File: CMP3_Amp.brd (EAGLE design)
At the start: 100 x 80 mm, 22 parts, among them J1 CONN_42.54_SCREW, J2 CONN_33.5_SCREW, Q2 DMG3404, U1 LTC2054, U2 LTC2054

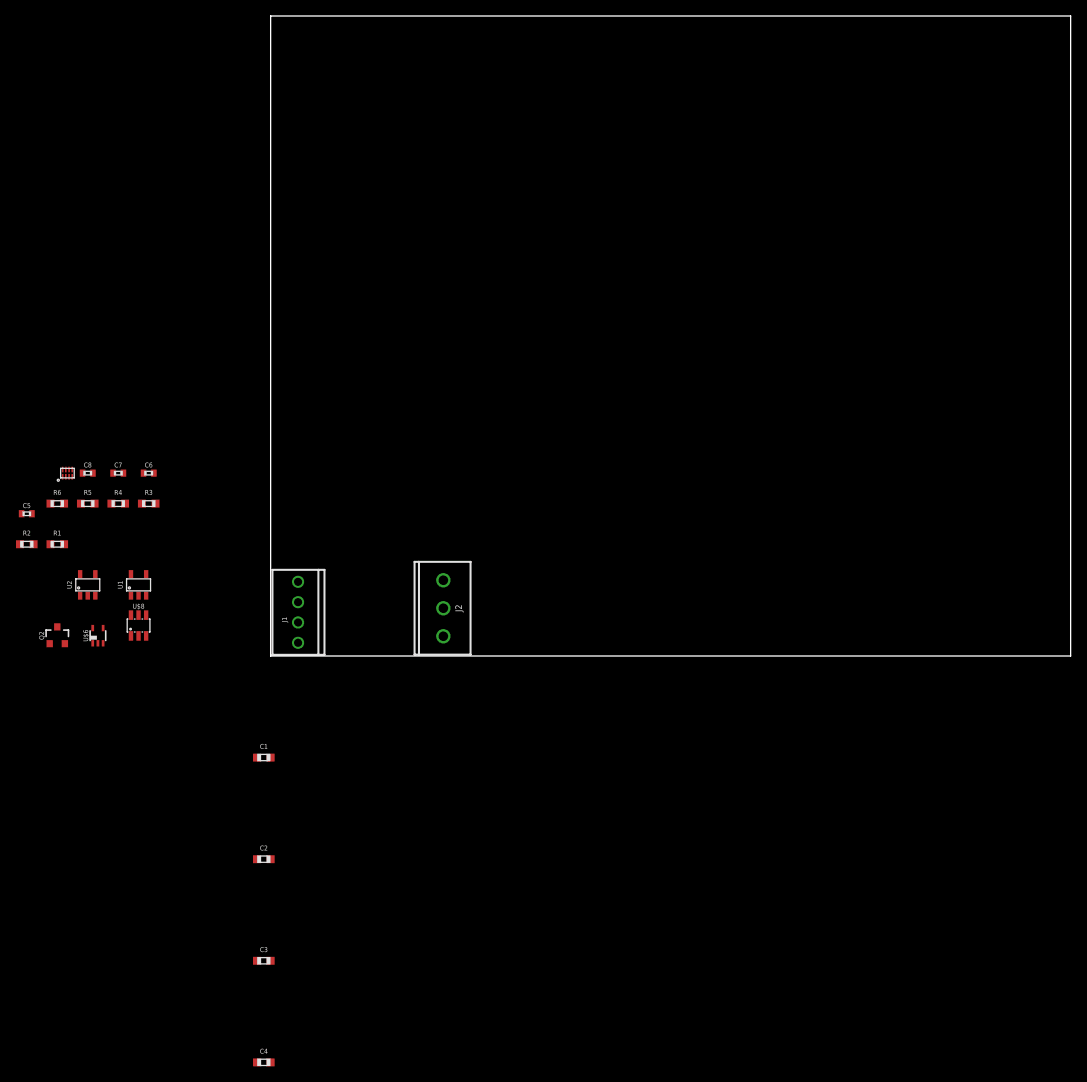
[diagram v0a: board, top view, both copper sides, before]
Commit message: Initial layout of CMP3 Amp
Layout of CMP3 amp complete, requires review and gerber generation before being sent to fab
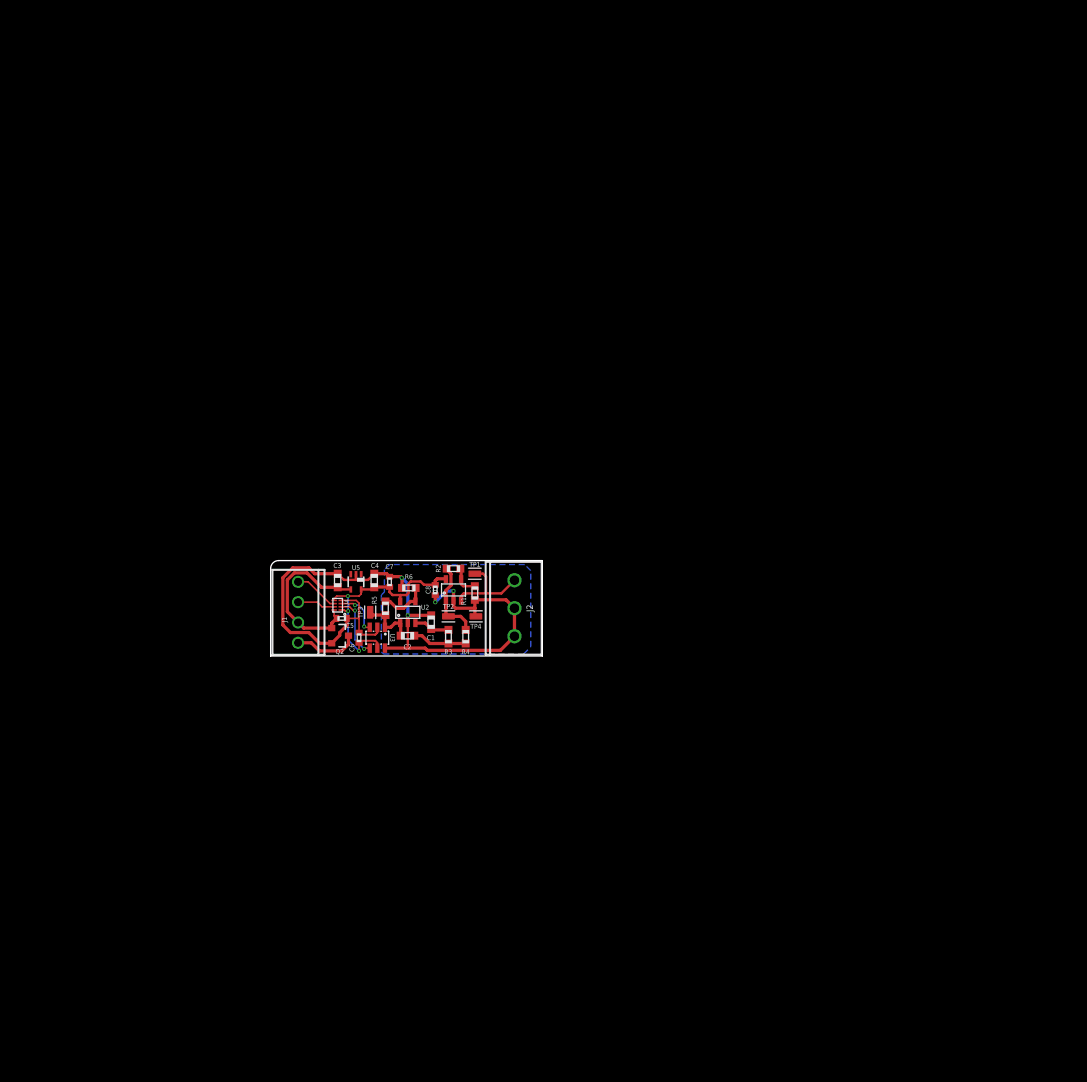
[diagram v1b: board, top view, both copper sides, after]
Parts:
- removed U$3: TXS0102DQM, bschulz:DQM_R-PX2SON-N8
- removed U$6: TPS79733, bschulz:DCK_R-PDSO-G5
- removed U$8: MCP3421A1, bschulz:SOT23-6L
- added TP1, TP2, TP3, TP4: TESTPOINTRCU, bschulz:TESTPOINT_0603
- added U3: MCP3421A1, bschulz:SOT23-6L
- added U4: TXS0102DQM, bschulz:DQM_R-PX2SON-N8
- added U5: TPS79733, bschulz:DCK_R-PDSO-G5
- moved C4 61.8 mm to (13.0, 9.44), turned to 90 degrees
- moved R2 53.4 mm to (22.9, 10.9)
- moved R1 52.6 mm to (25.5, 7.87), turned to 90 degrees
- moved C3 48.4 mm to (8.38, 9.44), turned to 90 degrees
- moved C8 45.8 mm to (20.6, 8.26), turned to 270 degrees
- moved R6 45.2 mm to (17.3, 8.51)
- moved R4 44.5 mm to (22.2, 2.41), turned to 270 degrees
- moved R3 43.0 mm to (24.4, 2.41), turned to 90 degrees
- moved C5 41.5 mm to (8.89, 4.70)
- moved U2 40.2 mm to (17.1, 5.46)
- moved R5 39.4 mm to (14.4, 5.97), turned to 270 degrees
- moved U1 39.4 mm to (22.9, 8.26)
- moved C7 36.5 mm to (14.9, 9.27), turned to 90 degrees
- moved Q2 35.3 mm to (8.64, 2.54), turned to 270 degrees
- moved C6 33.4 mm to (11.0, 2.29), turned to 90 degrees
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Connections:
- net 3V3: now also U3.5, U4.1, U4.5, U5.5; no longer U$3.1, U$3.5, U$6.5, U$8.5
- net GND: now also TP4.1, U3.2, U3.6, U4.4, U5.2; no longer U$3.4, U$6.2, U$8.2, U$8.6
- net SCL: now also U3.3, U4.3; no longer U$3.2, U$8.3
- net SCL_HV: now also U4.6; no longer U$3.7
- net SDA: now also U3.4, U4.2; no longer U$3.3, U$8.4
- net SDA_HV: now also U4.7; no longer U$3.6
- net VIN+: now also U4.8, U5.4; no longer U$3.8, U$6.4
- net VOUT_FILT: now also TP3.1, U3.1; no longer U$8.1
- net VOUT_GAIN: now also TP2.1
- net V_PYRO: now also TP1.1
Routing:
- net GND: track 0.00 -> 94.7 mm, vias 0 -> 4
- net 3V3: track 0.00 -> 31.4 mm, vias 0 -> 3
- net VIN+: track 0.00 -> 22.2 mm
- net V_PYRO: track 0.00 -> 11.7 mm
- net VOUT_GAIN: track 0.00 -> 10.1 mm
- net VIN-: track 0.00 -> 8.14 mm
- net SDA: track 0.00 -> 7.91 mm, vias 0 -> 2
- net VOUT_FILT: track 0.00 -> 7.33 mm
- net N$5: track 0.00 -> 6.83 mm
- net V_FB: track 0.00 -> 6.17 mm
- net SCL: track 0.00 -> 5.93 mm, vias 0 -> 2
- net SCL_HV: track 0.00 -> 5.63 mm
- net SDA_HV: track 0.00 -> 4.74 mm
- net N$6: track 0.00 -> 4.48 mm
- net N$2: track 0.00 -> 3.81 mm
- added copper zone on layer 16, net GND
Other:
- board size 100 x 80 mm -> 34 x 11.9 mm
- board text added: "(Blk)"
- board text added: "(Blue)"
- board text added: "(CMP3)"
- board text added: "(Red)"
- board text added: "3.3v ~ 5v"
- board text added: "CMP3 Amp v0.0 -------------- Designed by Northern Widget and University of Minnesota"
- board text added: "GND"
- board text added: "SCL"
- board text added: "SDA"
- board text added: "To Logger"
- board text added: "To Sensor"
- board text added: "Vin"
- board text added: "Vin+"
- board text added: "Vin-"
- board text added: "±"
